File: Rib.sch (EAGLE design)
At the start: 34 parts, among them IC1 REG1117, IC2 REG1117, SW1 DPDT, SW2 DPDT

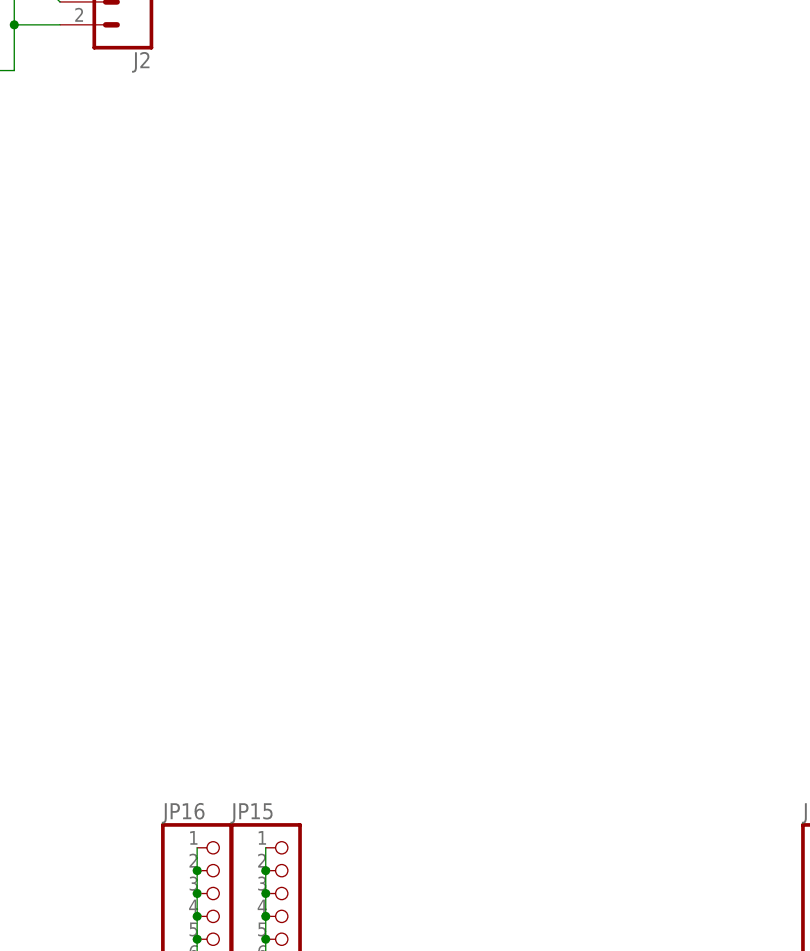
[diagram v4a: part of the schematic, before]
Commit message: Added Power, Fuse, Regulated satus LEDs
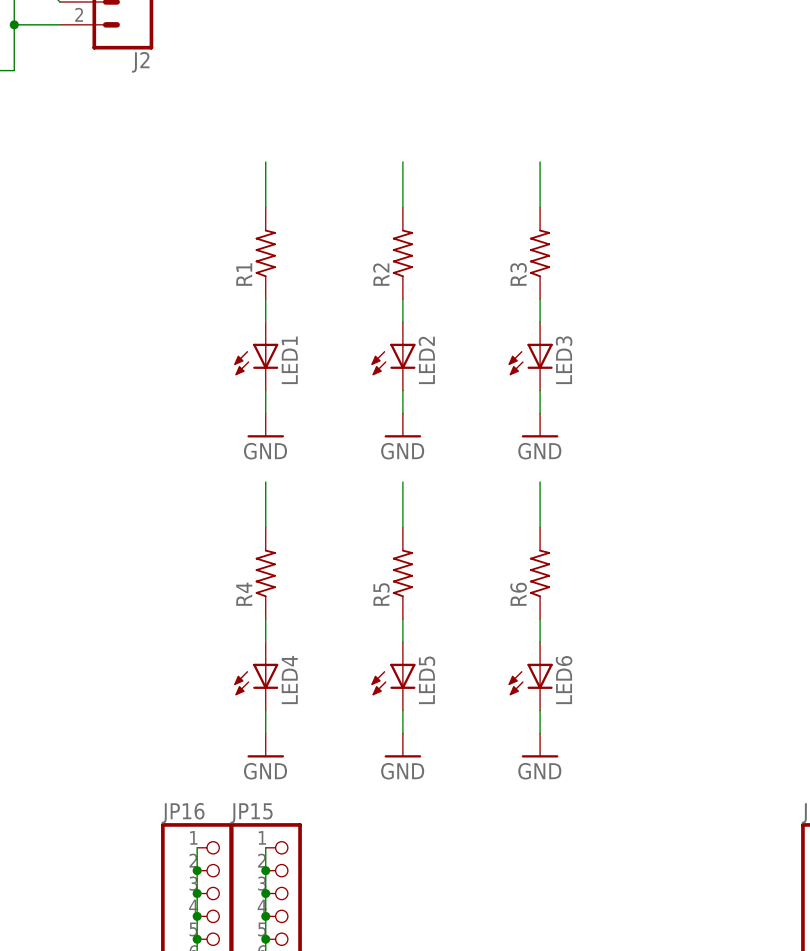
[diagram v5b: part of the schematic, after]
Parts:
- added LED1, LED2, LED3, LED4, LED5, LED6: (no value), eagle-ltspice:LED_ESML0603
- added R1, R2, R3, R4, R5, R6: (no value), resistor:R-US_R0603
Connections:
- new net N$24: LED1.A, R1.1
- new net N$37: LED2.A, R2.1
- new net N$38: LED3.A, R3.1
- new net N$40: LED4.A, R4.1
- new net N$41: LED5.A, R5.1
- new net N$42: LED6.A, R6.1
- net GND: now also LED1.C, LED2.C, LED3.C, LED4.C, LED5.C, LED6.C
- net LIPORAW: now also R2.2, R5.2
- net V3.3: now also R3.2, R6.2
- net VCC: now also R1.2, R4.2
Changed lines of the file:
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@@
 <part name="F3" library="3557-2" deviceset="3557-2" device=""/>
 <part name="F4" library="3557-2" deviceset="3557-2" device=""/>
+<part name="LED1" library="eagle-ltspice" library_urn="urn:adsk.eagle:library:217" deviceset="LED_E" device="SML0603" package3d_urn="urn:adsk.eagle:package:13315/1"/>
+<part name="LED2" library="eagle-ltspice" library_urn="urn:adsk.eagle:library:217" deviceset="LED_E" device="SML0603" package3d_urn="urn:adsk.eagle:package:13315/1"/>
+<part name="LED3" library="eagle-ltspice" library_urn="urn:adsk.eagle:library:217" deviceset="LED_E" device="SML0603" package3d_urn="urn:adsk.eagle:package:13315/1"/>
+<part name="GND12" library="supply1" library_urn="urn:adsk.eagle:library:371" deviceset="GND" device=""/>
+<part name="GND13" library="supply1" library_urn="urn:adsk.eagle:library:371" deviceset="GND" device=""/>
+<part name="GND14" library="supply1" library_urn="urn:adsk.eagle:library:371" deviceset="GND" device=""/>
+<part name="R1" library="resistor" library_urn="urn:adsk.eagle:library:348" deviceset="R-US_" device="R0603" package3d_urn="urn:adsk.eagle:package:26057/1"/>
+<part name="R2" library="resistor" library_urn="urn:adsk.eagle:library:348" deviceset="R-US_" device="R0603" package3d_urn="urn:adsk.eagle:package:26057/1"/>
+<part name="R3" library="resistor" library_urn="urn:adsk.eagle:library:348" deviceset="R-US_" device="R0603" package3d_urn="urn:adsk.eagle:package:26057/1"/>
+<part name="LED4" library="eagle-ltspice" library_urn="urn:adsk.eagle:library:217" deviceset="LED_E" device="SML0603" package3d_urn="urn:adsk.eagle:package:13315/1"/>
+<part name="LED5" library="eagle-ltspice" library_urn="urn:adsk.eagle:library:217" deviceset="LED_E" device="SML0603" package3d_urn="urn:adsk.eagle:package:13315/1"/>
+<part name="LED6" library="eagle-ltspice" library_urn="urn:adsk.eagle:library:217" deviceset="LED_E" device="SML0603" package3d_urn="urn:adsk.eagle:package:13315/1"/>
+<part name="GND15" library="supply1" library_urn="urn:adsk.eagle:library:371" deviceset="GND" device=""/>
+<part name="GND16" library="supply1" library_urn="urn:adsk.eagle:library:371" deviceset="GND" device=""/>
+<part name="GND17" library="supply1" library_urn="urn:adsk.eagle:library:371" deviceset="GND" device=""/>
+<part name="R4" library="resistor" library_urn="urn:adsk.eagle:library:348" deviceset="R-US_" device="R0603" package3d_urn="urn:adsk.eagle:package:26057/1"/>
+<part name="R5" library="resistor" library_urn="urn:adsk.eagle:library:348" deviceset="R-US_" device="R0603" package3d_urn="urn:adsk.eagle:package:26057/1"/>
+<part name="R6" library="resistor" library_urn="urn:adsk.eagle:library:348" deviceset="R-US_" device="R0603" package3d_urn="urn:adsk.eagle:package:26057/1"/>
 </parts>
 <sheets>
@@
 <instance part="F3" gate="G$1" x="30.48" y="-71.12"/>
 <instance part="F4" gate="G$1" x="30.48" y="-55.88"/>
+<instance part="LED1" gate="G$1" x="96.52" y="-111.76"/>
+<instance part="LED2" gate="G$1" x="111.76" y="-111.76"/>
+<instance part="LED3" gate="G$1" x="127" y="-111.76"/>
+<instance part="GND12" gate="1" x="96.52" y="-121.92"/>
+<instance part="GND13" gate="1" x="111.76" y="-121.92"/>
+<instance part="GND14" gate="1" x="127" y="-121.92"/>
+<instance part="R1" gate="G$1" x="96.52" y="-101.6" rot="R90"/>
+<instance part="R2" gate="G$1" x="111.76" y="-101.6" rot="R90"/>
+<instance part="R3" gate="G$1" x="127" y="-101.6" rot="R90"/>
+<instance part="LED4" gate="G$1" x="96.52" y="-147.32"/>
+<instance part="LED5" gate="G$1" x="111.76" y="-147.32"/>
+<instance part="LED6" gate="G$1" x="127" y="-147.32"/>
+<instance part="GND15" gate="1" x="96.52" y="-157.48"/>
+<instance part="GND16" gate="1" x="111.76" y="-157.48"/>
+<instance part="GND17" gate="1" x="127" y="-157.48"/>
+<instance part="R4" gate="G$1" x="96.52" y="-137.16" rot="R90"/>
+<instance part="R5" gate="G$1" x="111.76" y="-137.16" rot="R90"/>
+<instance part="R6" gate="G$1" x="127" y="-137.16" rot="R90"/>
 </instances>
 <busses>
@@
 <junction x="132.08" y="-276.86"/>
 </segment>
+<segment>
+<pinref part="LED3" gate="G$1" pin="C"/>
+<pinref part="GND14" gate="1" pin="GND"/>
+<wire x1="127" y1="-116.84" x2="127" y2="-119.38" width="0.1524" layer="91"/>
+</segment>
+<segment>
+<pinref part="LED2" gate="G$1" pin="C"/>
+<pinref part="GND13" gate="1" pin="GND"/>
+<wire x1="111.76" y1="-116.84" x2="111.76" y2="-119.38" width="0.1524" layer="91"/>
+</segment>
+<segment>
+<pinref part="LED1" gate="G$1" pin="C"/>
+<pinref part="GND12" gate="1" pin="GND"/>
+<wire x1="96.52" y1="-116.84" x2="96.52" y2="-119.38" width="0.1524" layer="91"/>
+</segment>
+<segment>
+<pinref part="LED6" gate="G$1" pin="C"/>
+<pinref part="GND17" gate="1" pin="GND"/>
+<wire x1="127" y1="-152.4" x2="127" y2="-154.94" width="0.1524" layer="91"/>
+</segment>
+<segment>
+<pinref part="LED5" gate="G$1" pin="C"/>
+<pinref part="GND16" gate="1" pin="GND"/>
+<wire x1="111.76" y1="-152.4" x2="111.76" y2="-154.94" width="0.1524" layer="91"/>
+</segment>
+<segment>
+<pinref part="LED4" gate="G$1" pin="C"/>
+<pinref part="GND15" gate="1" pin="GND"/>
+<wire x1="96.52" y1="-152.4" x2="96.52" y2="-154.94" width="0.1524" layer="91"/>
+</segment>
 </net>
 <net name="VCC" class="0">
@@
 <junction x="96.52" y="-223.52"/>
 </segment>
+<segment>
+<pinref part="R1" gate="G$1" pin="2"/>
+<wire x1="96.52" y1="-96.52" x2="96.52" y2="-91.44" width="0.1524" layer="91"/>
+</segment>
+<segment>
+<pinref part="R4" gate="G$1" pin="2"/>
+<wire x1="96.52" y1="-132.08" x2="96.52" y2="-127" width="0.1524" layer="91"/>
+</segment>
 </net>
 <net name="5V" class="0">
@@
 <junction x="58.42" y="-66.04"/>
 <pinref part="F4" gate="G$1" pin="P$2"/>
+</segment>
+<segment>
+<pinref part="R2" gate="G$1" pin="2"/>
+<wire x1="111.76" y1="-96.52" x2="111.76" y2="-91.44" width="0.1524" layer="91"/>
+</segment>
+<segment>
+<pinref part="R5" gate="G$1" pin="2"/>
+<wire x1="111.76" y1="-132.08" x2="111.76" y2="-127" width="0.1524" layer="91"/>
 </segment>
 </net>
@@
 <junction x="160.02" y="-223.52"/>
 </segment>
+<segment>
+<pinref part="R3" gate="G$1" pin="2"/>
+<wire x1="127" y1="-96.52" x2="127" y2="-91.44" width="0.1524" layer="91"/>
+</segment>
+<segment>
+<pinref part="R6" gate="G$1" pin="2"/>
+<wire x1="127" y1="-132.08" x2="127" y2="-127" width="0.1524" layer="91"/>
+</segment>
 </net>
 <net name="N$1" class="0">
@@
 <wire x1="132.08" y1="-335.28" x2="139.7" y2="-335.28" width="0.1524" layer="91"/>
 <junction x="132.08" y="-335.28"/>
+</segment>
+</net>
+<net name="N$24" class="0">
+<segment>
+<pinref part="R1" gate="G$1" pin="1"/>
+<pinref part="LED1" gate="G$1" pin="A"/>
+<wire x1="96.52" y1="-106.68" x2="96.52" y2="-109.22" width="0.1524" layer="91"/>
+</segment>
+</net>
+<net name="N$37" class="0">
+<segment>
+<pinref part="R2" gate="G$1" pin="1"/>
+<pinref part="LED2" gate="G$1" pin="A"/>
+<wire x1="111.76" y1="-106.68" x2="111.76" y2="-109.22" width="0.1524" layer="91"/>
+</segment>
+</net>
+<net name="N$38" class="0">
+<segment>
+<pinref part="R3" gate="G$1" pin="1"/>
+<pinref part="LED3" gate="G$1" pin="A"/>
+<wire x1="127" y1="-106.68" x2="127" y2="-109.22" width="0.1524" layer="91"/>
+</segment>
+</net>
+<net name="N$40" class="0">
+<segment>
+<pinref part="R4" gate="G$1" pin="1"/>
+<pinref part="LED4" gate="G$1" pin="A"/>
+<wire x1="96.52" y1="-142.24" x2="96.52" y2="-144.78" width="0.1524" layer="91"/>
+</segment>
+</net>
+<net name="N$41" class="0">
+<segment>
+<pinref part="R5" gate="G$1" pin="1"/>
+<pinref part="LED5" gate="G$1" pin="A"/>
+<wire x1="111.76" y1="-142.24" x2="111.76" y2="-144.78" width="0.1524" layer="91"/>
+</segment>
+</net>
+<net name="N$42" class="0">
+<segment>
+<pinref part="R6" gate="G$1" pin="1"/>
+<pinref part="LED6" gate="G$1" pin="A"/>
+<wire x1="127" y1="-142.24" x2="127" y2="-144.78" width="0.1524" layer="91"/>
 </segment>
 </net>
@@
 with this version.
 </note>
+<note version="8.3" severity="warning">
+Since Version 8.3, EAGLE supports URNs for individual library
+assets (packages, symbols, and devices). The URNs of those assets
+will not be understood (or retained) with this version.
+</note>
+<note version="8.3" severity="warning">
+Since Version 8.3, EAGLE supports the association of 3D packages
+with devices in libraries, schematics, and board files. Those 3D
+packages will not be understood (or retained) with this version.
+</note>
 </compatibility>
